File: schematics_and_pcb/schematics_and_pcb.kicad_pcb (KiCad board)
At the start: 2 copper layers, 123.5 x 90 mm, 77 parts, among them J1 RND 205-00623, J2 RND 205-00627, J3 Motor con, Q1 PMV213SN, SW1 RND 210-00210, U1 MIC5235YM5-TR, U2 AP2125N-3.3TRG1, U3 PWM3389DM-T3QU, U4 STM32F411RETx, Y1 YLFXTAL029370

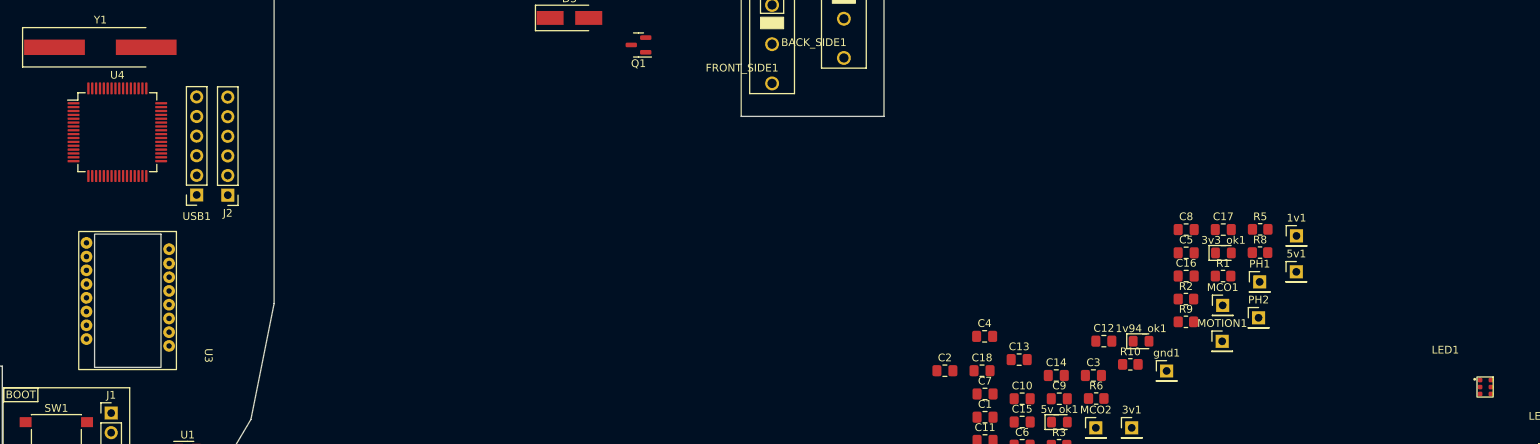
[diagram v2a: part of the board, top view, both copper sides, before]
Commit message: some highspeed signal traces
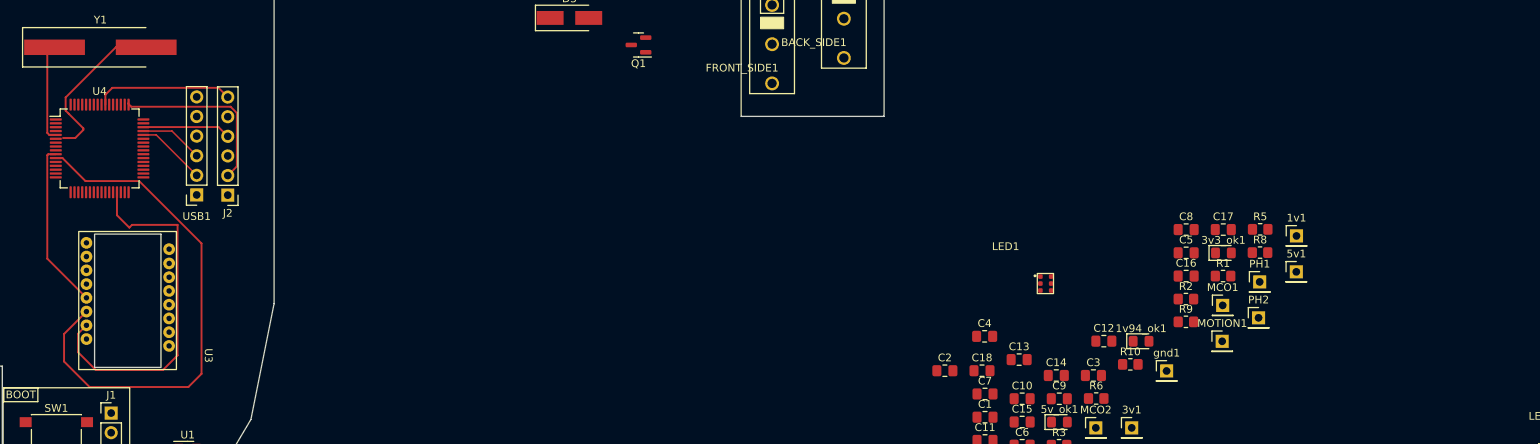
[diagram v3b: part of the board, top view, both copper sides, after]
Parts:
- moved LED1 58.5 mm to (160.9, 78.9)
- moved U4 3.11 mm to (38.4, 61.4)
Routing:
- net SPI2_MOSI: track 0.00 -> 67.9 mm
- net SPI2_SCK: track 0.00 -> 47.1 mm
- net SWDCLK: track 0.00 -> 23.3 mm
- net SPI2_MISO: track 0.00 -> 21.7 mm
- net PH1: track 0.00 -> 21.4 mm
- net SWO: track 0.00 -> 18.0 mm
- net PH0: track 0.00 -> 12.7 mm
- net SWDIO: track 0.00 -> 11.4 mm
- net D-: track 0.00 -> 9.07 mm
- net D+: track 0.00 -> 8.22 mm
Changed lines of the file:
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@@
   )
   (footprint "Package_QFP:LQFP-64_10x10mm_P0.5mm" (layer "F.Cu")
-    (at 40.7 59.3)
+    (at 38.4 61.4)
     (descr "LQFP, 64 Pin (https://www.analog.com/media/en/technical-documentation/data-sheets/ad7606_7606-6_7606-4.pdf), generated with kicad-footprint-generator ipc_gullwing_generator.py")
     (tags "LQFP QFP")
@@
   )
   (footprint "mouse:RND_135-00249" (layer "F.Cu")
-    (at 217.9 92.3)
+    (at 160.95 78.9)
     (property "Sheetfile" "schematics_and_pcb.kicad_sch")
     (property "Sheetname" "")
@@
     (effects (font (size 1 1) (thickness 0.15)))
   )
+  (segment (start 32.5625 48.3) (end 31.62548 49.23702) (width 0.25) (layer "F.Cu") (net 10))
+  (segment (start 31.62548 59.390486) (end 31.884994 59.65) (width 0.25) (layer "F.Cu") (net 10))
+  (segment (start 31.884994 59.65) (end 32.725 59.65) (width 0.25) (layer "F.Cu") (net 10))
+  (segment (start 31.62548 49.23702) (end 31.62548 59.390486) (width 0.25) (layer "F.Cu") (net 10))
+  (segment (start 40.5 48.3) (end 34 54.8) (width 0.25) (layer "F.Cu") (net 11))
+  (segment (start 44.4375 48.3) (end 40.5 48.3) (width 0.25) (layer "F.Cu") (net 11))
+  (segment (start 36.3 58.8) (end 36.3 59) (width 0.25) (layer "F.Cu") (net 11))
+  (segment (start 36.3 59) (end 35.250489 60.049511) (width 0.25) (layer "F.Cu") (net 11))
+  (segment (start 34 54.8) (end 34 56.5) (width 0.25) (layer "F.Cu") (net 11))
+  (segment (start 35.250489 60.049511) (end 33.665495 60.049511) (width 0.25) (layer "F.Cu") (net 11))
+  (segment (start 34 56.5) (end 34.4 56.9) (width 0.25) (layer "F.Cu") (net 11))
+  (segment (start 34.4 56.9) (end 36.3 58.8) (width 0.25) (layer "F.Cu") (net 11))
+  (segment (start 42.12452 55.62452) (end 42.12452 55.5) (width 0.25) (layer "F.Cu") (net 14))
+  (segment (start 56.174511 63.735489) (end 56.174511 56.803501) (width 0.25) (layer "F.Cu") (net 14))
+  (segment (start 55.37101 56) (end 42.5 56) (width 0.25) (layer "F.Cu") (net 14))
+  (segment (start 42.5 56) (end 42.12452 55.62452) (width 0.25) (layer "F.Cu") (net 14))
+  (segment (start 56.174511 56.803501) (end 55.37101 56) (width 0.25) (layer "F.Cu") (net 14))
+  (segment (start 55 64.91) (end 56.174511 63.735489) (width 0.25) (layer "F.Cu") (net 14))
+  (segment (start 53.800489 58.630489) (end 44.094511 58.630489) (width 0.25) (layer "F.Cu") (net 15))
+  (segment (start 55 59.83) (end 53.800489 58.630489) (width 0.25) (layer "F.Cu") (net 15))
+  (segment (start 44.094511 58.630489) (end 44.075 58.65) (width 0.25) (layer "F.Cu") (net 15))
+  (segment (start 55 54.75) (end 53.800489 53.550489) (width 0.25) (layer "F.Cu") (net 16))
+  (segment (start 40.049511 53.550489) (end 39.15 54.45) (width 0.25) (layer "F.Cu") (net 16))
+  (segment (start 39.15 54.45) (end 39.15 55.725) (width 0.25) (layer "F.Cu") (net 16))
+  (segment (start 53.800489 53.550489) (end 40.049511 53.550489) (width 0.25) (layer "F.Cu") (net 16))
+  (segment (start 31.62548 62.27452) (end 31.75 62.15) (width 0.25) (layer "F.Cu") (net 22))
+  (segment (start 31.75 62.15) (end 32.725 62.15) (width 0.25) (layer "F.Cu") (net 22))
+  (segment (start 31.62548 75.67548) (end 31.62548 62.27452) (width 0.25) (layer "F.Cu") (net 22))
+  (segment (start 36.7 80.75) (end 31.62548 75.67548) (width 0.25) (layer "F.Cu") (net 22))
+  (segment (start 33.8 89) (end 37.1 92.3) (width 0.25) (layer "F.Cu") (net 28))
+  (segment (start 51.6 90.6) (end 51.6 73.7) (width 0.25) (layer "F.Cu") (net 28))
+  (segment (start 43.52452 65.62452) (end 36.574031 65.62452) (width 0.25) (layer "F.Cu") (net 28))
+  (segment (start 51.6 73.7) (end 43.52452 65.62452) (width 0.25) (layer "F.Cu") (net 28))
+  (segment (start 49.9 92.3) (end 51.6 90.6) (width 0.25) (layer "F.Cu") (net 28))
+  (segment (start 33.8 85.43) (end 33.8 89) (width 0.25) (layer "F.Cu") (net 28))
+  (segment (start 33.599511 62.65) (end 32.725 62.65) (width 0.25) (layer "F.Cu") (net 28))
+  (segment (start 36.7 82.53) (end 33.8 85.43) (width 0.25) (layer "F.Cu") (net 28))
+  (segment (start 37.1 92.3) (end 49.9 92.3) (width 0.25) (layer "F.Cu") (net 28))
+  (segment (start 36.574031 65.62452) (end 33.599511 62.65) (width 0.25) (layer "F.Cu") (net 28))
+  (segment (start 48.5 88.2) (end 48.5 71.3) (width 0.25) (layer "F.Cu") (net 42))
+  (segment (start 42.25 71.65) (end 40.65 70.05) (width 0.25) (layer "F.Cu") (net 42))
+  (segment (start 48.5 71.3) (end 42.6 71.3) (width 0.25) (layer "F.Cu") (net 42))
+  (segment (start 42.6 71.3) (end 42.25 71.65) (width 0.25) (layer "F.Cu") (net 42))
+  (segment (start 46.6 90.1) (end 48.5 88.2) (width 0.25) (layer "F.Cu") (net 42))
+  (segment (start 40.65 70.05) (end 40.65 67.075) (width 0.25) (layer "F.Cu") (net 42))
+  (segment (start 35.613489 87.800293) (end 37.913196 90.1) (width 0.25) (layer "F.Cu") (net 42))
+  (segment (start 35.613489 85.396511) (end 35.613489 87.800293) (width 0.25) (layer "F.Cu") (net 42))
+  (segment (start 37.913196 90.1) (end 46.6 90.1) (width 0.25) (layer "F.Cu") (net 42))
+  (segment (start 36.7 84.31) (end 35.613489 85.396511) (width 0.25) (layer "F.Cu") (net 42))
+  (segment (start 45.74 59.65) (end 44.075 59.65) (width 0.2) (layer "F.Cu") (net 51))
+  (segment (start 50.975 64.885) (end 45.74 59.65) (width 0.2) (layer "F.Cu") (net 51))
+  (segment (start 50.975 62.345) (end 47.78 59.15) (width 0.2) (layer "F.Cu") (net 52))
+  (segment (start 47.78 59.15) (end 44.075 59.15) (width 0.2) (layer "F.Cu") (net 52))
 )

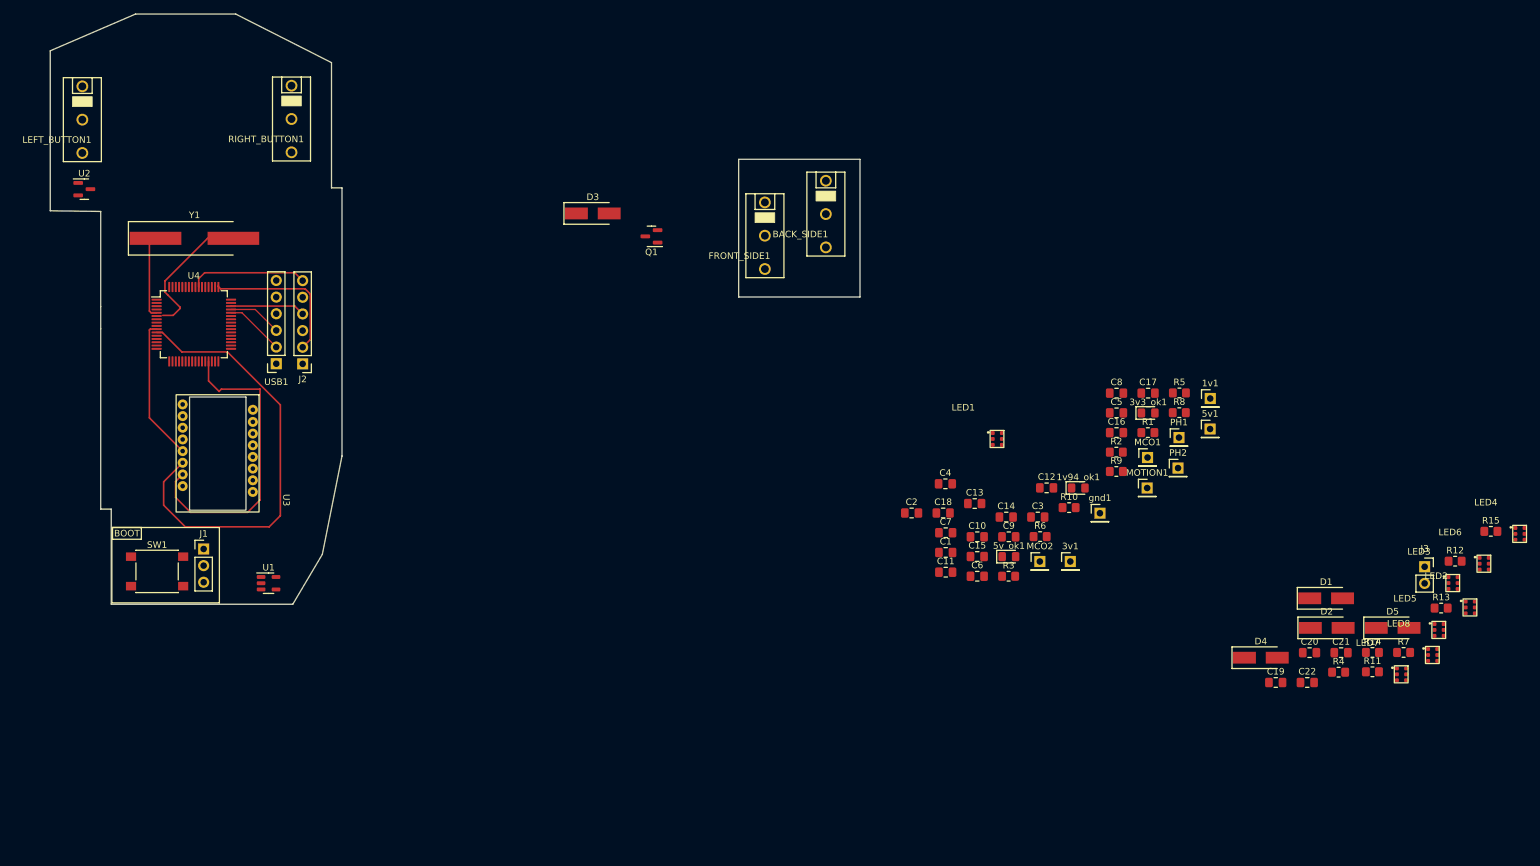
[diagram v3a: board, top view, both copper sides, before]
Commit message: layout of main board almost done
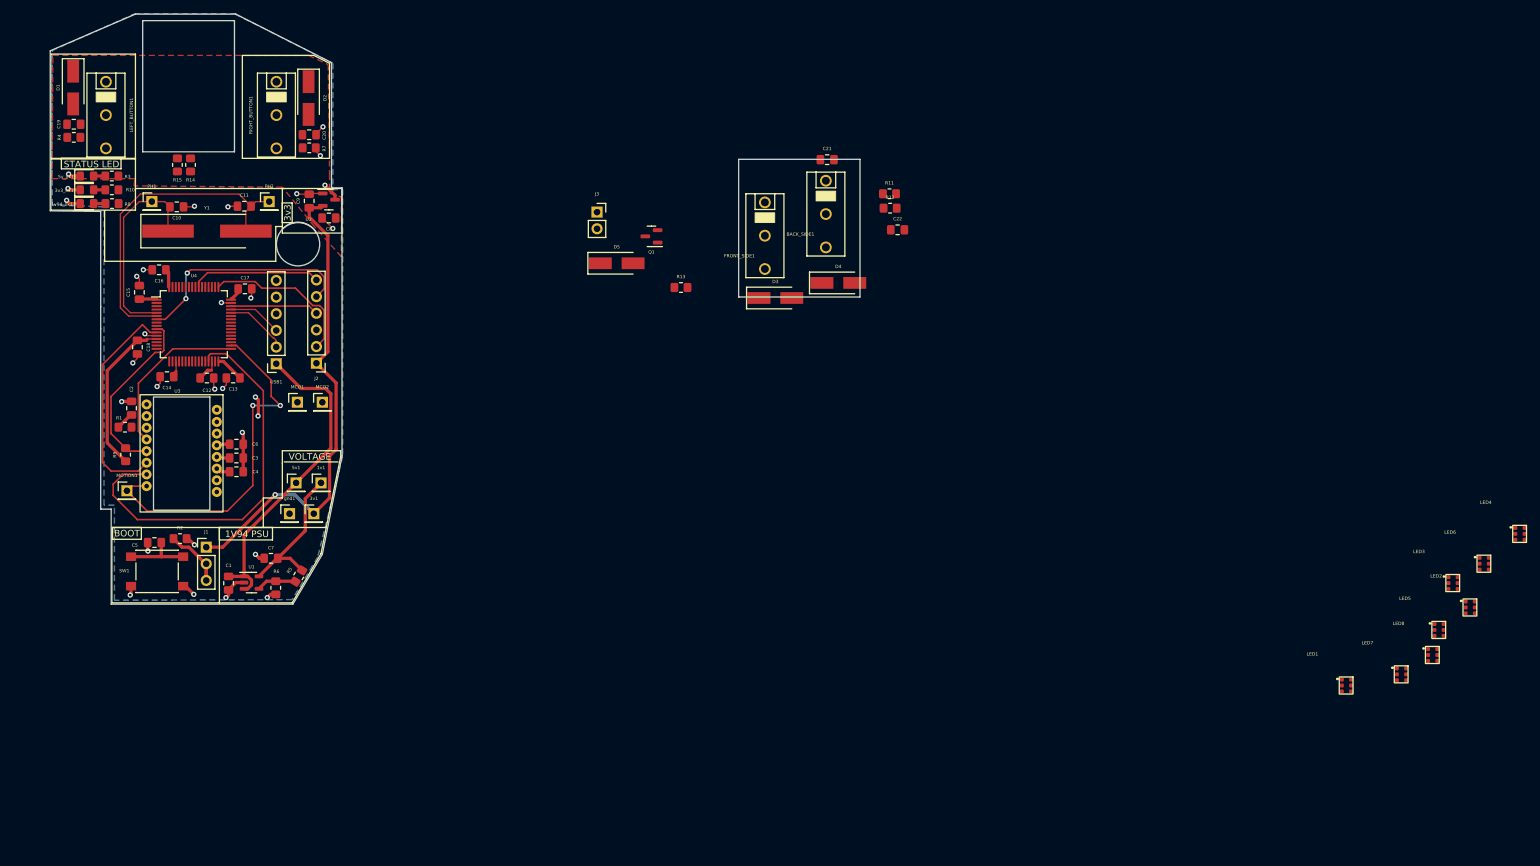
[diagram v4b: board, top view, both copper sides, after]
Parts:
- moved R4 209.4 mm to (20.1, 32.9), turned to 180 degrees
- moved R15 208.0 mm to (35.9, 37.1), turned to -90 degrees
- moved D1 206.4 mm to (20.0, 25.3), turned to -90 degrees
- moved C19 202.1 mm to (20.1, 30.9), turned to 180 degrees
- moved R14 195.0 mm to (37.9, 37.1), turned to -90 degrees
- moved R7 183.8 mm to (56.0, 34.5), turned to 180 degrees
- moved D2 175.1 mm to (55.9, 26.9), turned to -90 degrees
- moved C20 171.8 mm to (56.0, 32.5), turned to 180 degrees
- moved R8 165.9 mm to (25.9, 43.0), turned to 180 degrees
- moved 3v3_ok1 165.4 mm to (22.1, 40.9)
- moved PH1 160.7 mm to (32.0, 42.7)
- moved 1v94_ok1 157.3 mm to (22.1, 43.0)
- moved R1 156.0 mm to (27.9, 77.1)
- moved MOTION1 155.6 mm to (28.2, 86.8)
- moved R10 153.8 mm to (25.9, 40.9), turned to 180 degrees
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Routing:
- net VDDIO: track 0.00 -> 115.1 mm, vias 0 -> 1
- net GND: track 0.00 -> 57.9 mm, vias 0 -> 29
- net MOTION: track 0.00 -> 54.6 mm, vias 0 -> 2
- net +5V: track 0.00 -> 52.3 mm, vias 0 -> 1
- net NRST: track 0.00 -> 44.9 mm, vias 0 -> 2
- net SPI2_MOSI: track 67.9 -> 34.0 mm
- net PH1: track 21.4 -> 49.5 mm
- net VDD: track 0.00 -> 27.5 mm
- net SPI2_NCS: track 0.00 -> 25.4 mm
- net PH0: track 12.7 -> 31.2 mm
- net SPI2_SCK: track 47.1 -> 61.3 mm
- net BOOT0: track 0.00 -> 11.6 mm
- net SPI2_MISO: track 21.7 -> 28.1 mm
- net Net-(R5-Pad1): track 0.00 -> 6.05 mm
- net Net-(C12-Pad1): track 0.00 -> 3.60 mm
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- added copper zone on F.Cu, net +5V
- added copper zone on B.Cu, net GND
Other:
- outline, holes or cut-outs redrawn
- board text added: "1V94 PSU"
- board text added: "3v3"
- board text added: "MOUSEWHEEL STUFF"
- board text added: "STATUS LED"
- board text added: "VOLTAGE"

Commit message: new layout
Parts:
- removed BACK_SIDE1, FRONT_SIDE1: D2F-01F, mouse:D2F-01F
- removed C21, C22: 10u, Capacitor_SMD:C_0805_2012Metric_Pad1.18x1.45mm_HandSolder
- removed D3, D4: S1A, Diode_SMD:D_SMA_Handsoldering
- removed LED1, LED2, LED3, LED4, LED5, LED6, LED7, LED8: RND_135-00249, mouse:RND_135-00249
- removed R11, R12: 4.7k, Resistor_SMD:R_0805_2012Metric_Pad1.20x1.40mm_HandSolder
- moved R3 112.7 mm to (78.8, 138.3), turned to 90 degrees
- moved 5v_ok1 111.2 mm to (78.8, 134.5), turned to -90 degrees
- moved R10 109.8 mm to (76.7, 138.3), turned to 90 degrees
- moved 3v3_ok1 108.3 mm to (76.7, 134.5), turned to -90 degrees
- moved R8 107.0 mm to (74.5, 138.3), turned to 90 degrees
- moved 1v94_ok1 105.5 mm to (74.5, 134.5), turned to -90 degrees
- moved R5 61.5 mm to (57.2, 38.4), turned to 149.4 degrees
- moved U2 60.7 mm to (48.0, 102.0), turned to 180 degrees
- moved R6 60.2 mm to (59.0, 41.9), turned to 180 degrees
- moved C9 59.5 mm to (51.0, 101.8), turned to -90 degrees
- moved U1 56.3 mm to (58.2, 45.6), turned to 90 degrees
- moved C8 55.2 mm to (48.0, 99.2), turned to 0 degrees
- moved J1 54.9 mm to (89.0, 70.0)
- moved C5 54.9 mm to (81.1, 69.3)
- moved R2 54.9 mm to (85.0, 68.8)
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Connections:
- U4 pad 2: unconnected-(U4-Pad2) -> RUMBLE
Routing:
- net VDDIO: track 115.1 -> 0.00 mm, vias 1 -> 0
- net SPI2_SCK: track 61.3 -> 0.00 mm
- net GND: track 57.9 -> 0.00 mm, vias 29 -> 0
- net MOTION: track 54.6 -> 0.00 mm, vias 2 -> 0
- net +5V: track 52.3 -> 0.00 mm, vias 1 -> 0
- net PH1: track 49.5 -> 0.00 mm
- net NRST: track 44.9 -> 0.00 mm, vias 2 -> 0
- net SPI2_MOSI: track 34.0 -> 0.00 mm
- net PH0: track 31.2 -> 0.00 mm
- net SPI2_MISO: track 28.1 -> 0.00 mm
- net VDD: track 27.5 -> 0.00 mm
- net SPI2_NCS: track 25.4 -> 0.00 mm
- net SWDCLK: track 24.3 -> 0.00 mm
- net SWO: track 19.8 -> 0.00 mm
- net SWDIO: track 13.5 -> 0.00 mm
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- removed copper zone on F.Cu, net +5V
- removed copper zone on B.Cu, net GND
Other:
- board size 123.5 x 90 mm -> 44.5 x 90 mm
- board text removed: "1V94 PSU"
- board text removed: "3v3"
- board text removed: "BOOT"
- board text removed: "STATUS LED"
- board text removed: "VOLTAGE"
